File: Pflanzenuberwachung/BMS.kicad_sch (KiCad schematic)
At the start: 23 parts, among them J7 USB_C_Receptacle_PowerOnly_6P, U4 LTC3553

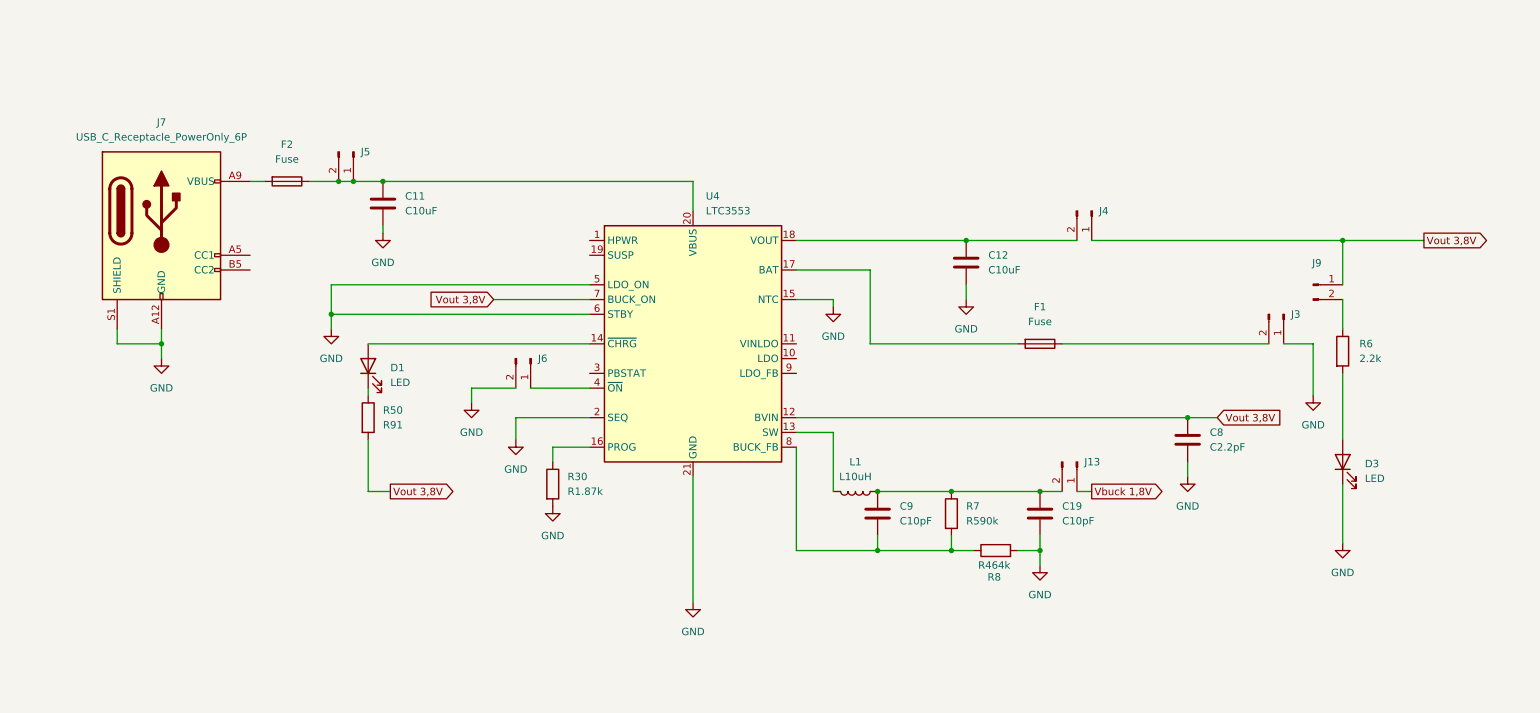
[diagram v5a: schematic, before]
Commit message: In Doku beschriebene Änderungen im Stromlaufplan eingefügt
Einfügen eins LDO für die Ausgangsspannung des BMS
Status LED für den Microprozessor
Ändern des MOSDED für die Sensoren von High Side zu Low Side
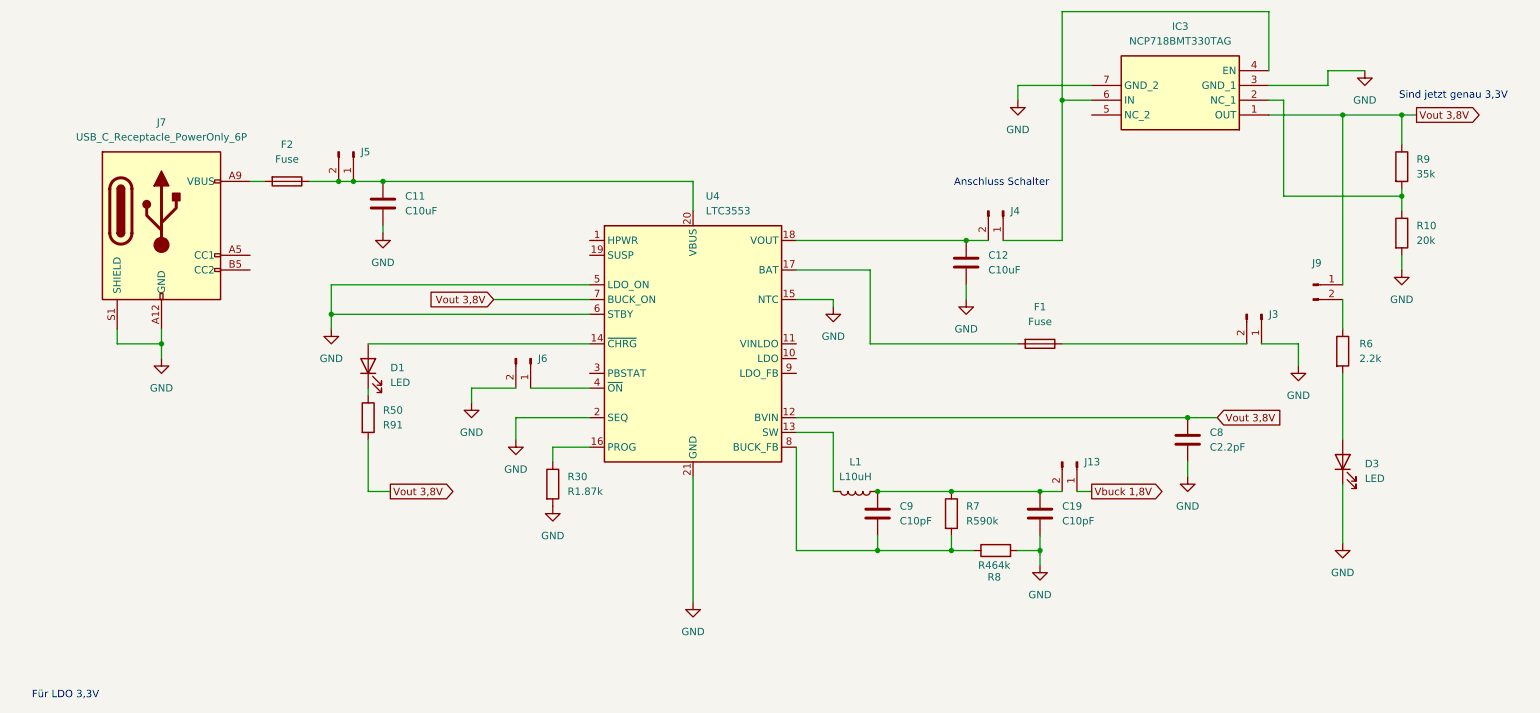
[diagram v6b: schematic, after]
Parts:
- added IC3: NCP718BMT330TAG, NCP718BMT330TAG, symbol Bauteile2:NCP718BMT330TAG
- added R10: 20k, Capacitor_SMD:C_0805_2012Metric, symbol Device:R
- added R9: 35k, Capacitor_SMD:C_0805_2012Metric, symbol Device:R
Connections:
- net GND: now also IC3.3 (GND_1), IC3.7 (GND_2), R10.2
- net Vout 3,8V: now also IC3.1 (OUT), R9.1; no longer J4.1 (Pin_1)
- new net: IC3.4 (EN), IC3.6 (IN), J4.1 (Pin_1)
- new net: IC3.2 (NC_1), R10.1, R9.2
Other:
- note added: "Anschluss Schalter"
- note added: "Für LDO 3,3V"
- note added: "Sind jetzt genau 3,3V"
- moved on the sheet: J3, J4
